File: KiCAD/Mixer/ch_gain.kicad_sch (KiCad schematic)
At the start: 8 parts, among them U1 NE5532

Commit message: Power Bus, Footprints, Audio Bus
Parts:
- R1, R2, R3: footprint (none) -> Resistor_SMD:R_0805_2012Metric_Pad1.20x1.40mm_HandSolder
- U1: footprint (none) -> Package_SO:SOIC-8_3.9x4.9mm_P1.27mm
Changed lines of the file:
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@@
 			)
 		)
-		(property "Footprint" ""
+		(property "Footprint" "Resistor_SMD:R_0805_2012Metric_Pad1.20x1.40mm_HandSolder"
 			(at 88.9 64.008 90)
 			(hide yes)
@@
 			)
 		)
-		(property "Footprint" ""
+		(property "Footprint" "Package_SO:SOIC-8_3.9x4.9mm_P1.27mm"
 			(at 88.9 83.82 0)
 			(hide yes)
@@
 			)
 		)
-		(property "Footprint" ""
+		(property "Footprint" "Package_SO:SOIC-8_3.9x4.9mm_P1.27mm"
 			(at 63.5 31.75 0)
 			(hide yes)
@@
 			)
 		)
-		(property "Footprint" ""
+		(property "Footprint" "Resistor_SMD:R_0805_2012Metric_Pad1.20x1.40mm_HandSolder"
 			(at 45.72 77.978 90)
 			(hide yes)
@@
 			)
 		)
-		(property "Footprint" ""
+		(property "Footprint" "Resistor_SMD:R_0805_2012Metric_Pad1.20x1.40mm_HandSolder"
 			(at 72.39 83.058 90)
 			(hide yes)

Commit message: added second channel and footprints / created PCB desing...might make PCB bit bigger
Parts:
- C2: footprint (none) -> Capacitor_SMD:C_0805_2012Metric_Pad1.18x1.45mm_HandSolder
- D1, D2: footprint (none) -> Diode_SMD:D_SOD-123
- RV1: value R_Potentiometer -> 10k; footprint (none) -> Potentiometer_THT:Potentiometer_Alps_RK09K_Single_Vertical
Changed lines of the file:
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@@
+					(unit 1)
+				)
+				(path "/322d427a-6aae-4762-92d6-d97688daf29b/8a2849b7-184d-4014-bb98-da9dec8b5f90/afbffc69-b100-46db-9180-c5285a610f62"
+					(reference "R15")
 					(unit 1)
 				)
@@
 					(unit 1)
 				)
+				(path "/322d427a-6aae-4762-92d6-d97688daf29b/8a2849b7-184d-4014-bb98-da9dec8b5f90/afbffc69-b100-46db-9180-c5285a610f62"
+					(reference "U2")
+					(unit 1)
+				)
 			)
 		)
@@
 					(unit 3)
 				)
+				(path "/322d427a-6aae-4762-92d6-d97688daf29b/8a2849b7-184d-4014-bb98-da9dec8b5f90/afbffc69-b100-46db-9180-c5285a610f62"
+					(reference "U2")
+					(unit 3)
+				)
 			)
 		)
@@
 					(unit 1)
 				)
+				(path "/322d427a-6aae-4762-92d6-d97688daf29b/8a2849b7-184d-4014-bb98-da9dec8b5f90/afbffc69-b100-46db-9180-c5285a610f62"
+					(reference "#PWR080")
+					(unit 1)
+				)
 			)
 		)
@@
 					(unit 1)
 				)
+				(path "/322d427a-6aae-4762-92d6-d97688daf29b/8a2849b7-184d-4014-bb98-da9dec8b5f90/afbffc69-b100-46db-9180-c5285a610f62"
+					(reference "#PWR078")
+					(unit 1)
+				)
 			)
 		)
@@
 					(unit 1)
 				)
+				(path "/322d427a-6aae-4762-92d6-d97688daf29b/8a2849b7-184d-4014-bb98-da9dec8b5f90/afbffc69-b100-46db-9180-c5285a610f62"
+					(reference "R13")
+					(unit 1)
+				)
 			)
 		)
@@
 			)
 		)
-		(property "Footprint" ""
+		(property "Footprint" "Capacitor_SMD:C_0805_2012Metric_Pad1.18x1.45mm_HandSolder"
 			(at 54.9148 24.13 0)
 			(hide yes)
@@
 				(path "/322d427a-6aae-4762-92d6-d97688daf29b/8a2849b7-184d-4014-bb98-da9dec8b5f90/874eb9e3-c612-43fb-9dc5-24309708e7ee"
 					(reference "C2")
+					(unit 1)
+				)
+				(path "/322d427a-6aae-4762-92d6-d97688daf29b/8a2849b7-184d-4014-bb98-da9dec8b5f90/afbffc69-b100-46db-9180-c5285a610f62"
+					(reference "C5")
 					(unit 1)
 				)
@@
 			)
 		)
-		(property "Value" "R_Potentiometer"
+		(property "Value" "10k"
 			(at 57.15 82.5499 0)
 			(show_name no)
@@
 			)
 		)
-		(property "Footprint" ""
+		(property "Footprint" "Potentiometer_THT:Potentiometer_Alps_RK09K_Single_Vertical"
 			(at 59.69 81.28 0)
 			(hide yes)
@@
 				(path "/322d427a-6aae-4762-92d6-d97688daf29b/8a2849b7-184d-4014-bb98-da9dec8b5f90/874eb9e3-c612-43fb-9dc5-24309708e7ee"
 					(reference "RV1")
+					(unit 1)
+				)
+				(path "/322d427a-6aae-4762-92d6-d97688daf29b/8a2849b7-184d-4014-bb98-da9dec8b5f90/afbffc69-b100-46db-9180-c5285a610f62"
+					(reference "RV5")
 					(unit 1)
 				)
@@
 					(unit 1)
 				)
+				(path "/322d427a-6aae-4762-92d6-d97688daf29b/8a2849b7-184d-4014-bb98-da9dec8b5f90/afbffc69-b100-46db-9180-c5285a610f62"
+					(reference "#PWR077")
+					(unit 1)
+				)
 			)
 		)
@@
 			)
 		)
-		(property "Footprint" ""
+		(property "Footprint" "Diode_SMD:D_SOD-123"
 			(at 88.9 66.04 0)
 			(hide yes)
@@
 				(path "/322d427a-6aae-4762-92d6-d97688daf29b/8a2849b7-184d-4014-bb98-da9dec8b5f90/874eb9e3-c612-43fb-9dc5-24309708e7ee"
 					(reference "D1")
+					(unit 1)
+				)
+				(path "/322d427a-6aae-4762-92d6-d97688daf29b/8a2849b7-184d-4014-bb98-da9dec8b5f90/afbffc69-b100-46db-9180-c5285a610f62"
+					(reference "D5")
 					(unit 1)
 				)
@@
 					(unit 1)
 				)
+				(path "/322d427a-6aae-4762-92d6-d97688daf29b/8a2849b7-184d-4014-bb98-da9dec8b5f90/afbffc69-b100-46db-9180-c5285a610f62"
+					(reference "R14")
+					(unit 1)
+				)
 			)
 		)
@@
 			)
 		)
-		(property "Footprint" ""
+		(property "Footprint" "Diode_SMD:D_SOD-123"
 			(at 88.9 69.85 0)
 			(hide yes)
@@
 				(path "/322d427a-6aae-4762-92d6-d97688daf29b/8a2849b7-184d-4014-bb98-da9dec8b5f90/874eb9e3-c612-43fb-9dc5-24309708e7ee"
 					(reference "D2")
+					(unit 1)
+				)
+				(path "/322d427a-6aae-4762-92d6-d97688daf29b/8a2849b7-184d-4014-bb98-da9dec8b5f90/afbffc69-b100-46db-9180-c5285a610f62"
+					(reference "D6")
 					(unit 1)
 				)
@@
 					(unit 1)
 				)
+				(path "/322d427a-6aae-4762-92d6-d97688daf29b/8a2849b7-184d-4014-bb98-da9dec8b5f90/afbffc69-b100-46db-9180-c5285a610f62"
+					(reference "#PWR079")
+					(unit 1)
+				)

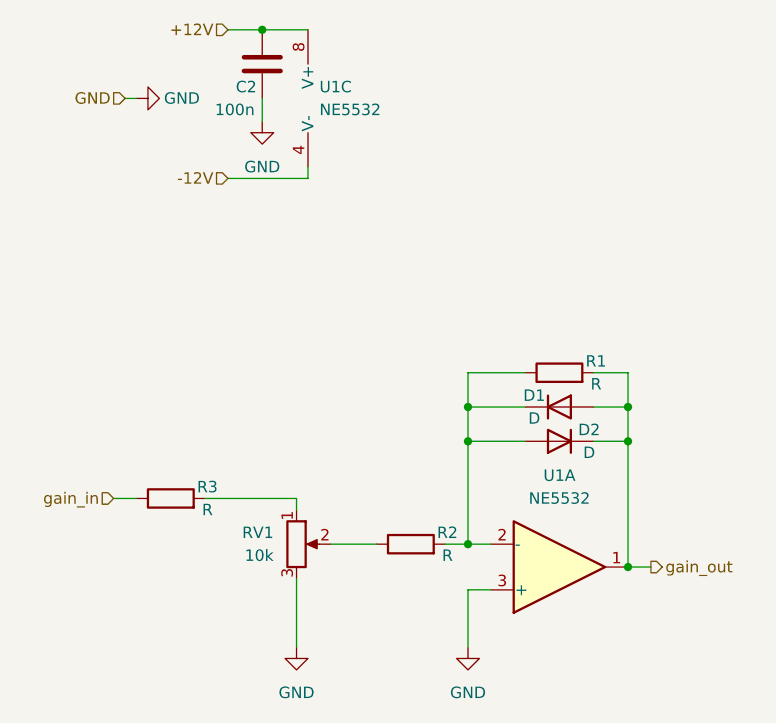
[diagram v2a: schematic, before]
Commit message: Cs an OPV-Strom, Anpassung clicklessmute,...
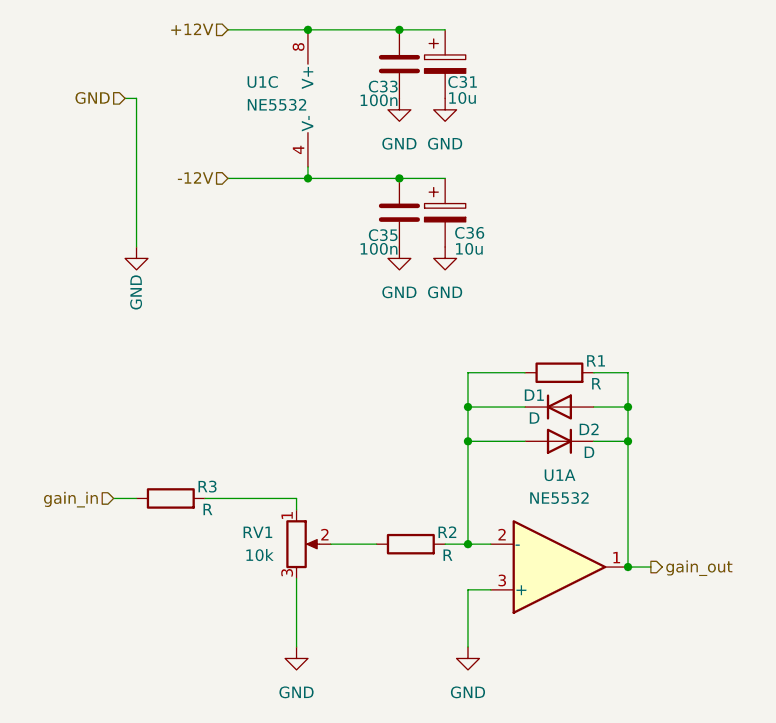
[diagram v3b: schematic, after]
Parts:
- removed C2: 100n, Capacitor_SMD:C_0805_2012Metric_Pad1.18x1.45mm_HandSolder, symbol Device:C
- added C31, C36: 10u, Capacitor_SMD:CP_Elec_10x10, symbol Device:C_Polarized
- added C33, C35: 100n, Capacitor_SMD:C_0805_2012Metric_Pad1.18x1.45mm_HandSolder, symbol Device:C
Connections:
- net +12V: now also C31.1, C33.2
- net -12V: now also C35.2, C36.1
- net GND: now also C31.2, C33.1, C35.1, C36.2

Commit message: überarbeitete Schaltung und PCB Desing...v1.0 FERTIG
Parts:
- removed C31, C36: 10u, Capacitor_SMD:CP_Elec_10x10, symbol Device:C_Polarized
- removed D1, D2: D, Diode_SMD:D_SOD-123, symbol Device:D
- added J4, J8: Conn_01x02_Socket, Connector_PinHeader_2.54mm:PinHeader_1x02_P2.54mm_Vertical, symbol Connector:Conn_01x02_Socket
- R1, R3: value R -> 10k
- R2: value R -> 1k
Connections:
- net gain_out: now also J4.2 (Pin_2), J8.2 (Pin_2)
- net at R1.1, R2.2, U1.2 (-): now also J4.1 (Pin_1), J8.1 (Pin_1)
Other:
- moved on the sheet: C33, C35, R1
